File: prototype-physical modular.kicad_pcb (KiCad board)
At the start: 2 copper layers, 100 x 164 mm, 177 parts, among them CON1 BARREL_JACK, CON2 SD_Card, IC1 ATMEGA2560-A, J1 MIDI_IN, J2 MIDI_OUT, P1 POWER, P13 PD, P15 PH, P16 PF, P17 SD_PINS, P18 3VI2C, P19 PIGPIO, P2 FTDI, P3 SPI, P4 BUSTI, P5 BUSTO, P7 PA, P9 PB, Q1 BSS138, Q2 BSS138, Q3 BSS138, Q4 BSS138, Q5 BSS138, Q6 BSS138, SW1 SW_PUSH, SW10 SW_PUSH, SW11 SW_PUSH, SW12 SW_PUSH, SW13 SW_PUSH, SW14 SW_PUSH, SW2 ROTARY_ENCODER_SWITCH, SW3 SW_PUSH, SW4 SW_PUSH, SW5 SW_PUSH, SW6 SW_PUSH, SW7 SW_PUSH, SW8 SW_PUSH, SW9 SW_PUSH, U1 NCP1117ST50T3G, U2 6N138, Y1 16MHz

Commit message: update gerbers
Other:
- board text added: "add more copper to power dissipation of power regulators"
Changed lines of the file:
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@@
     (area -9.7188 -6.191901 101.927 176.783501)
     (thickness 1.6)
-    (drawings 14)
+    (drawings 15)
     (tracks 3993)
     (zones 0)
@@
     (pad_to_mask_clearance 0.2)
     (aux_axis_origin 0 0)
-    (visible_elements 7FFFCFFF)
+    (visible_elements 7FFFDFFF)
     (pcbplotparams
       (layerselection 0x011fc_80000001)
@@
   (module lib_fp:ws2812_buttonPad (layer F.Cu)
     (at 0 100)
-    (fp_text reference WSB9 (at 1.17 -19.83 90) (layer F.SilkS) hide
+    (fp_text reference WSB9 (at 2.5 -37.5 90) (layer F.SilkS)
       (effects (font (thickness 0.15)))
     )
-    (fp_text value WS2812_BUTTON (at 1.17 -8.4 90) (layer F.SilkS) hide
+    (fp_text value WS2812_BUTTON (at 2.5 -7.5 90) (layer F.SilkS) hide
       (effects (font (thickness 0.15)))
     )
@@
     (fp_circle (center 12.2 -37.5) (end 19.7 -37.5) (layer F.Cu) (width 0.254))
     (fp_circle (center 12.21 -37.51) (end 16.71 -37.51) (layer F.Cu) (width 0.254))
-    (fp_text user C3 (at 19 -44) (layer F.SilkS)
+    (fp_text user C3 (at 8.9 -45.1) (layer F.SilkS) hide
       (effects (font (size 0.9652 0.9652) (thickness 0.1524)))
     )
@@
   (module lib_fp:ws2812_buttonPad (layer F.Cu)
     (at 25 100)
-    (fp_text reference WSB10 (at 1.17 -19.83 90) (layer F.SilkS) hide
+    (fp_text reference WSB10 (at 2.5 -37.5 90) (layer F.SilkS)
       (effects (font (thickness 0.15)))
     )
@@
     (fp_circle (center 12.2 -37.5) (end 19.7 -37.5) (layer F.Cu) (width 0.254))
     (fp_circle (center 12.21 -37.51) (end 16.71 -37.51) (layer F.Cu) (width 0.254))
-    (fp_text user C3 (at 19 -44) (layer F.SilkS)
+    (fp_text user C3 (at 19 -44) (layer F.SilkS) hide
       (effects (font (size 0.9652 0.9652) (thickness 0.1524)))
     )
@@
   (module lib_fp:ws2812_buttonPad (layer F.Cu)
     (at 50 100)
-    (fp_text reference WSB11 (at 2.023 -21 90) (layer F.SilkS) hide
+    (fp_text reference WSB11 (at 2.5 -37.5 90) (layer F.SilkS)
       (effects (font (thickness 0.15)))
     )
@@
     (fp_circle (center 12.2 -37.5) (end 19.7 -37.5) (layer F.Cu) (width 0.254))
     (fp_circle (center 12.21 -37.51) (end 16.71 -37.51) (layer F.Cu) (width 0.254))
-    (fp_text user C3 (at 19 -44) (layer F.SilkS)
+    (fp_text user C3 (at 19 -44) (layer F.SilkS) hide
       (effects (font (size 0.9652 0.9652) (thickness 0.1524)))
     )
@@
   (module lib_fp:ws2812_buttonPad (layer F.Cu)
     (at 75 100)
-    (fp_text reference WSB12 (at 1.17 -2.5 90) (layer F.SilkS) hide
+    (fp_text reference WSB12 (at 2.5 -37.5 90) (layer F.SilkS)
       (effects (font (thickness 0.15)))
     )
-    (fp_text value WS2812_BUTTON (at 1.17 -8.4 90) (layer F.SilkS) hide
+    (fp_text value WS2812_BUTTON (at 5 -8.4 90) (layer F.SilkS) hide
       (effects (font (thickness 0.15)))
     )
@@
     (fp_circle (center 12.2 -37.5) (end 19.7 -37.5) (layer F.Cu) (width 0.254))
     (fp_circle (center 12.21 -37.51) (end 16.71 -37.51) (layer F.Cu) (width 0.254))
-    (fp_text user C3 (at 19 -44) (layer F.SilkS)
+    (fp_text user C3 (at 19 -44) (layer F.SilkS) hide
       (effects (font (size 0.9652 0.9652) (thickness 0.1524)))
     )
@@
   (module lib_fp:ws2812_buttonPad (layer F.Cu)
     (at 0 125)
-    (fp_text reference WSB13 (at 1.17 -19.83 90) (layer F.SilkS) hide
+    (fp_text reference WSB13 (at 2.5 -37.5 90) (layer F.SilkS)
       (effects (font (thickness 0.15)))
     )
@@
   (module lib_fp:ws2812_buttonPad (layer F.Cu)
     (at 25 125)
-    (fp_text reference WSB14 (at 1.17 -19.83 90) (layer F.SilkS) hide
+    (fp_text reference WSB14 (at 2.5 -37.5 90) (layer F.SilkS)
       (effects (font (thickness 0.15)))
     )
@@
   (module lib_fp:ws2812_buttonPad (layer F.Cu)
     (at 50 125)
-    (fp_text reference WSB15 (at 1.17 -19.83 90) (layer F.SilkS) hide
+    (fp_text reference WSB15 (at 2.5 -37.5 90) (layer F.SilkS)
       (effects (font (thickness 0.15)))
     )
@@
   (module lib_fp:ws2812_buttonPad (layer F.Cu)
     (at 75 125)
-    (fp_text reference WSB16 (at 1.17 -19.83 90) (layer F.SilkS) hide
+    (fp_text reference WSB16 (at 2.5 -37.5 90) (layer F.SilkS)
       (effects (font (thickness 0.15)))
     )
@@
     (fp_circle (center 12.2 -37.5) (end 19.7 -37.5) (layer F.Cu) (width 0.254))
     (fp_circle (center 12.21 -37.51) (end 16.71 -37.51) (layer F.Cu) (width 0.254))
-    (fp_text user C3 (at 19 -44) (layer F.SilkS)
+    (fp_text user C3 (at 19 -44) (layer F.SilkS) hide
       (effects (font (size 0.9652 0.9652) (thickness 0.1524)))
     )
@@
   (module lib_fp:ws2812_buttonPad (layer F.Cu)
     (at 0 150)
-    (fp_text reference WSB17 (at 2.023 -17 90) (layer F.SilkS) hide
+    (fp_text reference WSB17 (at 2.5 -37.5 90) (layer F.SilkS)
       (effects (font (thickness 0.15)))
     )
@@
   (module lib_fp:ws2812_buttonPad (layer F.Cu)
     (at 24.977 150)
-    (fp_text reference WSB18 (at 1.17 -19.83 90) (layer F.SilkS) hide
+    (fp_text reference WSB18 (at 2.523 -37.5 90) (layer F.SilkS)
       (effects (font (thickness 0.15)))
     )
@@
   (module lib_fp:ws2812_buttonPad (layer F.Cu)
     (at 50 150)
-    (fp_text reference WSB19 (at 1.17 -19.83 90) (layer F.SilkS) hide
+    (fp_text reference WSB19 (at 2.5 -37.5 90) (layer F.SilkS)
       (effects (font (thickness 0.15)))
     )
@@
   (module lib_fp:ws2812_buttonPad (layer F.Cu)
     (at 75 150)
-    (fp_text reference WSB20 (at 1.17 -19.83 90) (layer F.SilkS) hide
+    (fp_text reference WSB20 (at 2.5 -37.5 90) (layer F.SilkS)
       (effects (font (thickness 0.15)))
     )
@@
   (module lib_fp:ws2812_buttonPad (layer F.Cu)
     (at 0 175)
-    (fp_text reference WSB21 (at 1.17 -19.83 90) (layer F.SilkS) hide
+    (fp_text reference WSB21 (at 2.5 -37.5 90) (layer F.SilkS)
       (effects (font (thickness 0.15)))
     )
@@
   (module lib_fp:ws2812_buttonPad (layer F.Cu)
     (at 25 175)
-    (fp_text reference WSB22 (at 1.17 -19.83 90) (layer F.SilkS) hide
+    (fp_text reference WSB22 (at 2.5 -37.5 90) (layer F.SilkS)
       (effects (font (thickness 0.15)))
     )
@@
   (module lib_fp:ws2812_buttonPad (layer F.Cu)
     (at 50 175)
-    (fp_text reference WSB23 (at 1.17 -19.83 90) (layer F.SilkS) hide
+    (fp_text reference WSB23 (at 2.5 -37.5 90) (layer F.SilkS)
       (effects (font (thickness 0.15)))
     )
@@
   (module lib_fp:ws2812_buttonPad (layer F.Cu)
     (at 75 175)
-    (fp_text reference WSB24 (at 1.17 -19.83 90) (layer F.SilkS) hide
+    (fp_text reference WSB24 (at 2.5 -37.5 90) (layer F.SilkS)
       (effects (font (thickness 0.15)))
     )
@@
     )
   )
+  (gr_text "add more copper to power dissipation of power regulators\n" (at 50.6 -17.7) (layer F.Cu)
+    (effects (font (size 1.5 1.5) (thickness 0.3)))
+  )
   (gr_line (start 98.5 164) (end 100 162.5) (layer Edge.Cuts) (width 0.15))

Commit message: annotation of some mistakes in board
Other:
- board text added: "error: keep clear of tracks where there are nuts!"
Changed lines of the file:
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@@
     (links 471)
     (no_connects 0)
-    (area -9.7188 -6.191901 101.927 176.783501)
+    (area -9.7188 -18.9 101.927 176.783501)
     (thickness 1.6)
-    (drawings 15)
+    (drawings 23)
     (tracks 3993)
     (zones 0)
@@
       (drillshape 0)
       (scaleselection 1)
-      (outputdirectory gerber/))
+      (outputdirectory prints/))
   )
   (net 0 "")
@@
     )
   )
+  (gr_circle (center 47.9 97.2) (end 115.5 91.9) (layer F.Mask) (width 0.2))
+  (gr_circle (center 3.2 52.6) (end -8 54.5) (layer F.Mask) (width 0.2))
+  (gr_circle (center 2.2 146.8) (end -5 140.8) (layer F.Mask) (width 0.2))
+  (gr_circle (center 2.7 102.1) (end -7 107.6) (layer F.Mask) (width 0.2))
+  (gr_circle (center 98.3 102.1) (end 107.7 106.1) (layer F.Mask) (width 0.2))
+  (gr_circle (center 97.2 52.5) (end 108.1 56.8) (layer F.Mask) (width 0.2))
+  (gr_circle (center 97.7 147.2) (end 103.6 149) (layer F.Mask) (width 0.2))
+  (gr_text "error: keep clear of tracks where there are nuts!" (at 132.3 138.5) (layer B.SilkS)
+    (effects (font (size 1.5 1.5) (thickness 0.3)))
+  )
   (gr_text "add more copper to power dissipation of power regulators\n" (at 50.6 -17.7) (layer F.Cu)

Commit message: test and add pulldowns for buttons
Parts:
- removed MUXA1, MUXB1: 4051, Housings_SSOP:SSOP-16_3.9x4.9mm_Pitch0.635mm
- removed uP1: ARDUPROMINI, ArduProMiniTKB:ArduProMini
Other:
- board text added: "move tacts, and choose better quality"

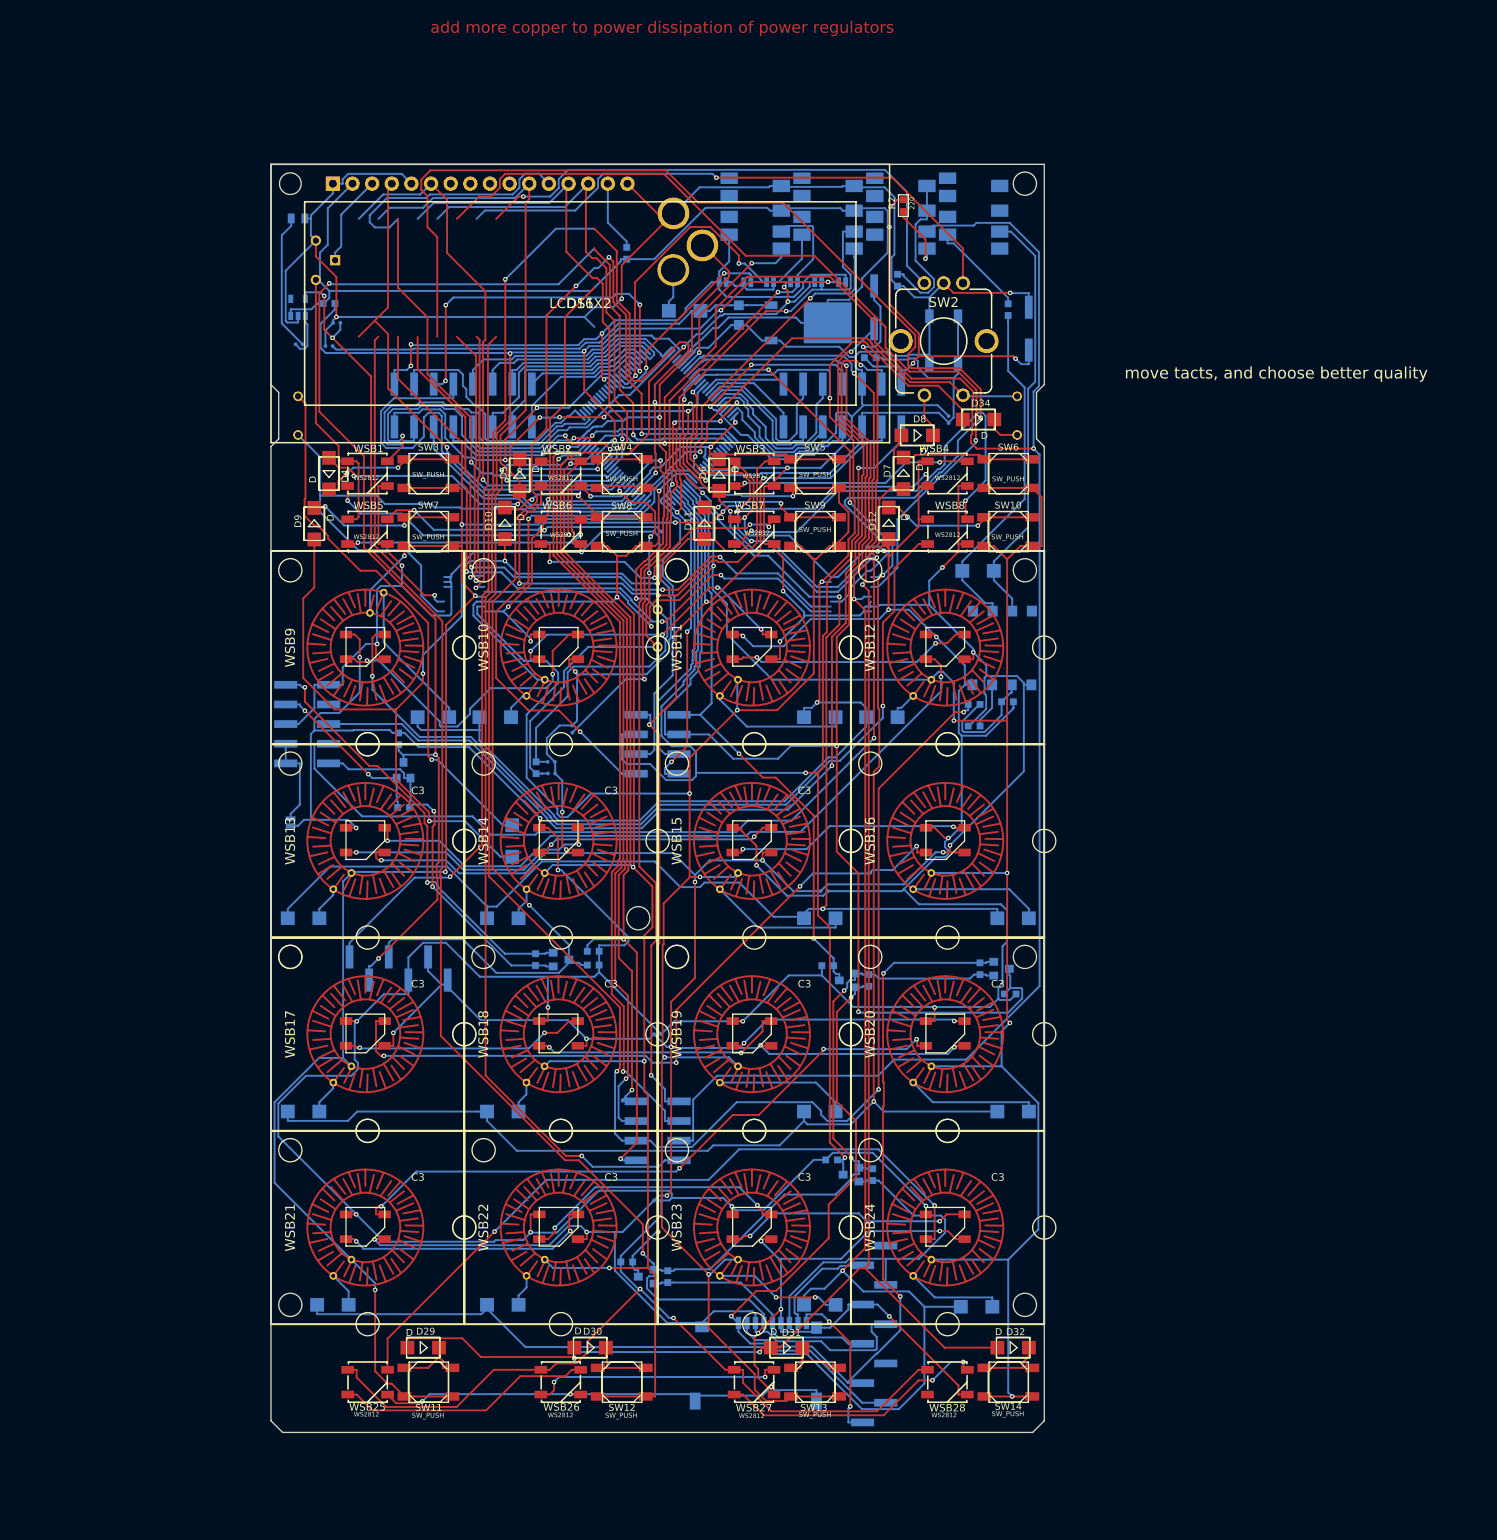
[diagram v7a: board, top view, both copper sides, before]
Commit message: flip bus with +5V pins in the BUSTO &BUSTI plugs otherwise, it does a shortcircuit sometimes when plugging the jack in.
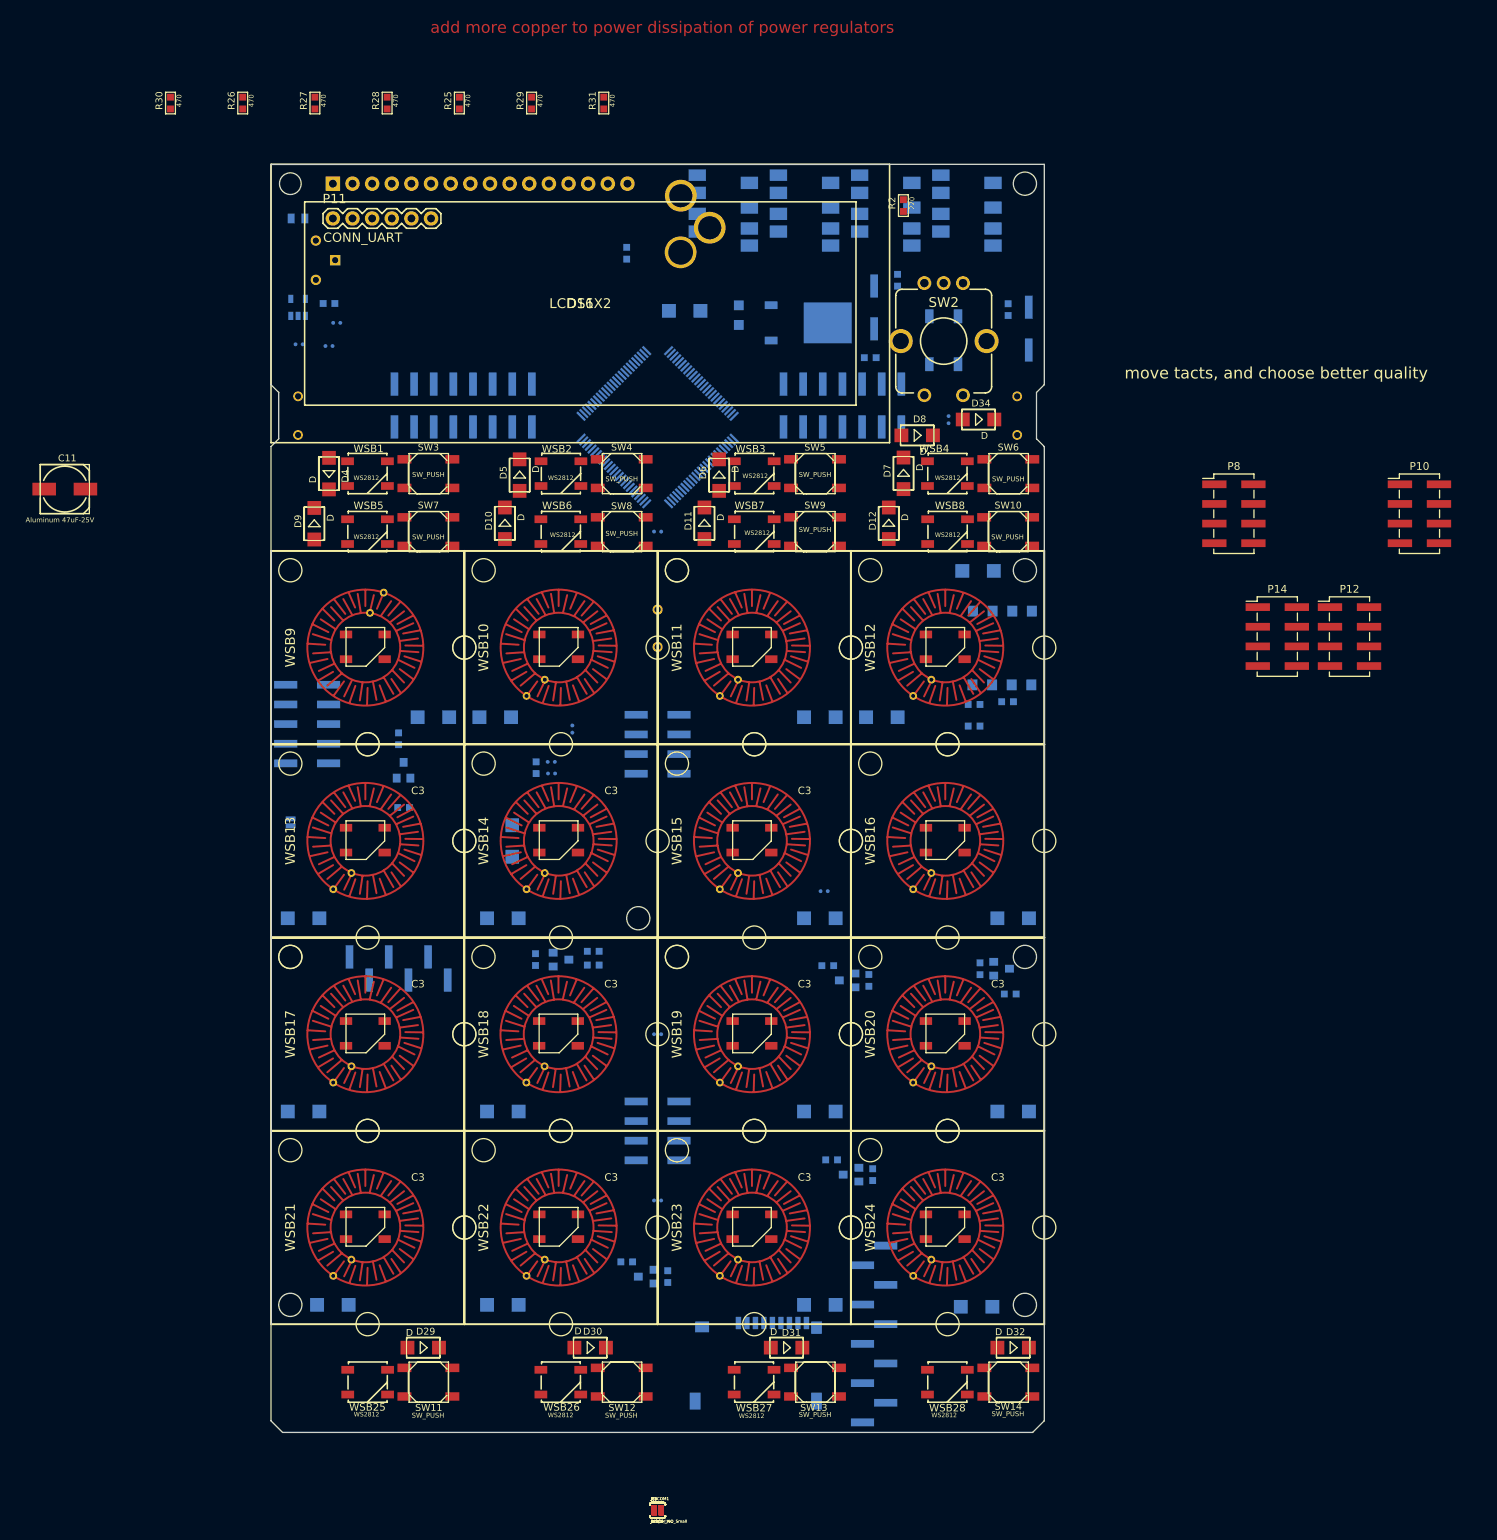
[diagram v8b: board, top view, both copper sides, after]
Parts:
- removed J1: MIDI_IN, SeeedOPL-Connector:AUDIO8P-SMD-3.5-14.5X6.1X4.0MM
- removed J2: MIDI_OUT, SeeedOPL-Connector:AUDIO8P-SMD-3.5-14.5X6.1X4.0MM
- removed P4: BUSTI, SeeedOPL-Connector:AUDIO8P-SMD-3.5-14.5X6.1X4.0MM
- removed P5: BUSTO, SeeedOPL-Connector:AUDIO8P-SMD-3.5-14.5X6.1X4.0MM
- added C11: Aluminum 47uF-25V, SeeedOPL-Capacitor:ELECTRO-SMD-C-6MM, F.Cu at (-26.7, 42.0)
- added P10: PC, Pin_Headers:Pin_Header_Straight_2x04_Pitch2.54mm_SMD, F.Cu at (148.5, 45.2)
- added P11: CONN_UART, SparkFun-Connectors:1X06, F.Cu at (8.00, 7.00)
- added P12: PJ, Pin_Headers:Pin_Header_Straight_2x04_Pitch2.54mm_SMD, F.Cu at (139.5, 61.1)
- added P14: PE, Pin_Headers:Pin_Header_Straight_2x04_Pitch2.54mm_SMD, F.Cu at (130.1, 61.1)
- added P20: MIDI_IN, SeeedOPL-Connector:AUDIO8P-SMD-3.5-14.5X6.1X4.0MM, B.Cu at (90.0, -1.50)
- added P21: MIDI_OUT, SeeedOPL-Connector:AUDIO8P-SMD-3.5-14.5X6.1X4.0MM, B.Cu at (79.5, -1.50)
- added P22: BUSTI, SeeedOPL-Connector:AUDIO8P-SMD-3.5-14.5X6.1X4.0MM, B.Cu at (58.5, -1.50)
- added P23: BUSTO, SeeedOPL-Connector:AUDIO8P-SMD-3.5-14.5X6.1X4.0MM, B.Cu at (69.0, -1.50)
- added P8: PL, Pin_Headers:Pin_Header_Straight_2x04_Pitch2.54mm_SMD, F.Cu at (124.5, 45.2)
- added R25: 470, SeeedOPL-Resistor:R0603, F.Cu at (24.4, -7.92)
- added R26: 470, SeeedOPL-Resistor:R0603, F.Cu at (-3.66, -7.92)
- added R27: 470, SeeedOPL-Resistor:R0603, F.Cu at (5.68, -7.92)
- added R28: 470, SeeedOPL-Resistor:R0603, F.Cu at (15.0, -7.92)
- added R29: 470, SeeedOPL-Resistor:R0603, F.Cu at (33.7, -7.92)
- added R30: 470, SeeedOPL-Resistor:R0603, F.Cu at (-13.0, -7.92)
- added R31: 470, SeeedOPL-Resistor:R0603, F.Cu at (43.0, -7.92)
- JP1, JP3, JP4, JP5, PJ1COM1, PJ2COM1: moved to F.Cu
- moved JP3 160.6 mm to (50.0, 174.1)
- moved JP5 160.2 mm to (50.0, 174.1)
- moved JP4 159.8 mm to (50.0, 174.1)
- moved PJ2COM1 159.5 mm to (50.0, 174.1), turned to 0 degrees
- moved PJ1COM1 159.3 mm to (50.0, 174.1)
- moved JP1 159.1 mm to (50.0, 174.1)
- moved CON1 2.48 mm to (53.0, -2.50)
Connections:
- IC1 pad 23: Net-(IC1-Pad23) -> /ENCA
- IC1 pad 26: Net-(IC1-Pad26) -> /ENCC
- P9 pad 5: Net-(IC1-Pad23) -> /ENCA
- P9 pad 8: Net-(IC1-Pad26) -> /ENCC
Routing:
- net GND: track 1029.1 -> 0.00 mm, vias 36 -> 0
- net +5V: track 1004.9 -> 0.00 mm, vias 30 -> 0
- net +3V3: track 275.0 -> 0.00 mm, vias 5 -> 0
- net /MUXAX3: track 273.6 -> 0.00 mm, vias 6 -> 0
- net /MUXBX5: track 266.5 -> 0.00 mm, vias 3 -> 0
- net /MIDI_OUT_TX: track 258.8 -> 0.00 mm, vias 2 -> 0
- net /MUXAX2: track 253.5 -> 0.00 mm, vias 6 -> 0
- net /RESET: track 245.9 -> 0.00 mm, vias 6 -> 0
- net /MUXBX6: track 232.6 -> 0.00 mm, vias 4 -> 0
- net /MUXAX1: track 220.8 -> 0.00 mm, vias 5 -> 0
- net /SDA: track 218.8 -> 0.00 mm, vias 6 -> 0
- net /MUXBX4: track 215.2 -> 0.00 mm, vias 4 -> 0
- net /MUXAX0: track 213.8 -> 0.00 mm, vias 5 -> 0
- net /MIDI_RX: track 202.4 -> 0.00 mm, vias 4 -> 0
- net /MUXBX3: track 189.1 -> 0.00 mm, vias 4 -> 0
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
